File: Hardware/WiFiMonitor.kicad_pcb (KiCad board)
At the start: 2 copper layers, 47.2 x 47.1 mm, 41 parts, among them J1 ADAP_ESP, J2 FTDI, J3 BATT, U1 4N25, U2 4N25, U3 4N25, U4 4N25, U5 U5, U6 AP1117-33, U7 DS3231MZ+

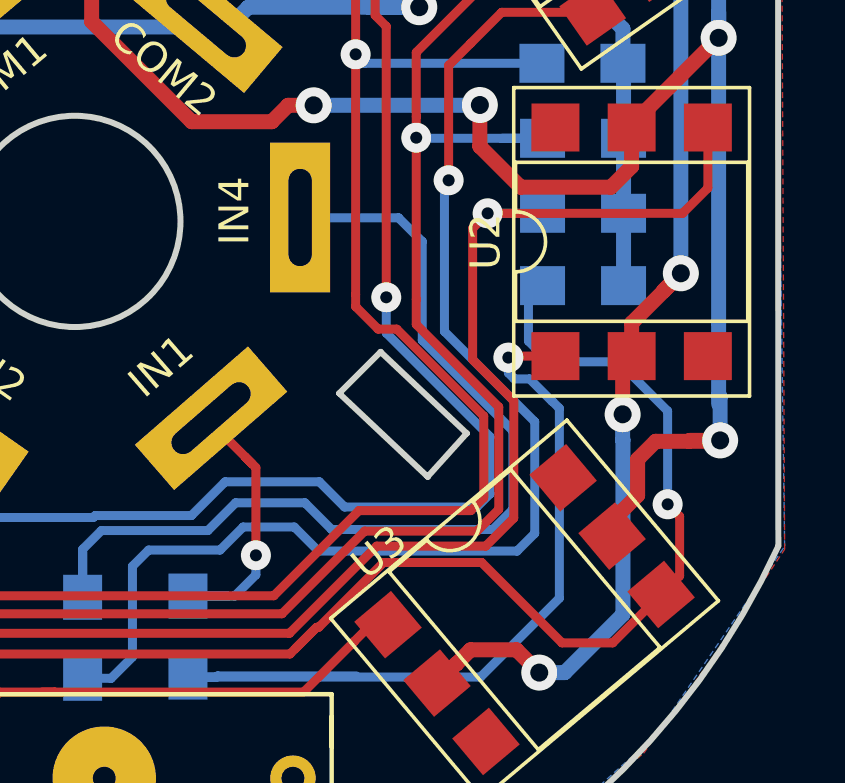
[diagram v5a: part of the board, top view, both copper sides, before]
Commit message: pads4_22
move
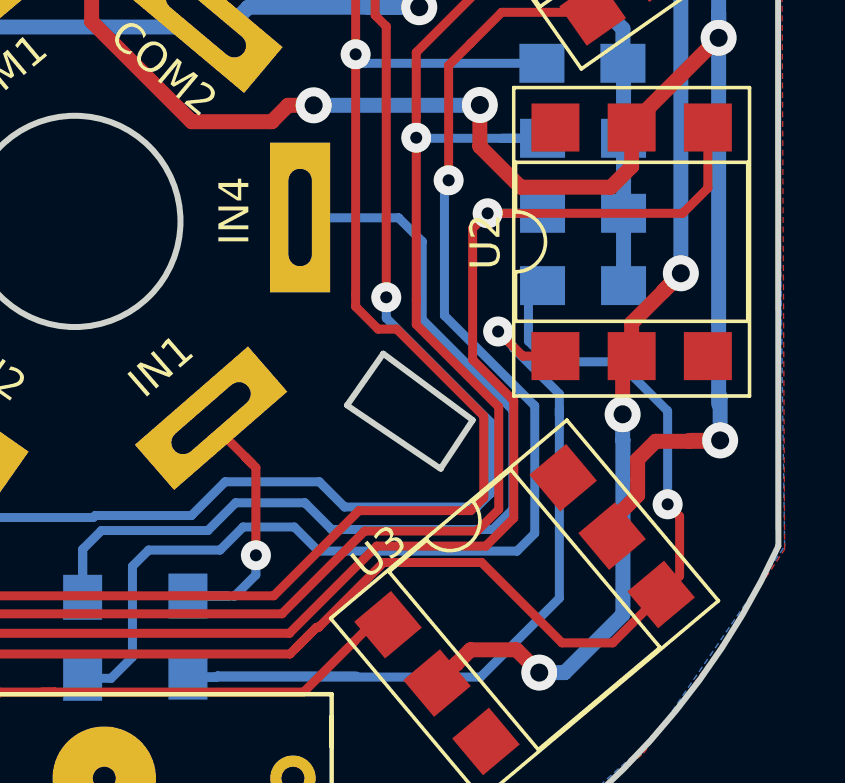
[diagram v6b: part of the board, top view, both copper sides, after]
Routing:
- net Net-(R4-Pad1): track 29.7 -> 31.3 mm
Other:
- outline, holes or cut-outs redrawn
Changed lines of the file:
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@@
     (links 70)
     (no_connects 2)
-    (area 125.549999 67.068854 174.355 116.145)
+    (area 126.056132 67.439999 173.398541 114.790001)
     (thickness 1.6)
     (drawings 29)
-    (tracks 647)
+    (tracks 646)
     (zones 0)
     (modules 41)
@@
   (gr_line (start 136.86 85.59) (end 139.46 87.58) (layer Edge.Cuts) (width 0.2))
   (gr_line (start 136.85 85.59) (end 139.16 82.2) (layer Edge.Cuts) (width 0.2))
-  (gr_line (start 160.0443 95.4057) (end 158.66 96.79) (layer Edge.Cuts) (width 0.2))
-  (gr_line (start 162.92 98.13) (end 160.04 95.41) (layer Edge.Cuts) (width 0.2))
-  (gr_line (start 161.61 99.57) (end 162.91684 98.12062) (layer Edge.Cuts) (width 0.2))
-  (gr_line (start 158.66 96.79) (end 161.62 99.58) (layer Edge.Cuts) (width 0.2))
+  (gr_line (start 160.13 95.47) (end 158.93 97.18) (layer Edge.Cuts) (width 0.2))
+  (gr_line (start 163.11 97.68) (end 160.13 95.47) (layer Edge.Cuts) (width 0.2))
+  (gr_line (start 162.05 99.29) (end 163.11 97.69) (layer Edge.Cuts) (width 0.2))
+  (gr_line (start 158.92 97.19) (end 162.05 99.31) (layer Edge.Cuts) (width 0.2))
   (gr_arc (start 149.72226 91.05258) (end 162.56 113.69) (angle 4.704154906) (layer Edge.Cuts) (width 0.2))
   (gr_arc (start 149.77814 91.05258) (end 173.29854 101.88568) (angle 28.7) (layer Edge.Cuts) (width 0.2))
@@
   (segment (start 140.22 91.07) (end 141.74 91.07) (width 0.3) (layer B.Cu) (net 12))
   (segment (start 150.11 103.59) (end 150.11 101.99) (width 0.3) (layer B.Cu) (net 13))
-  (segment (start 161.43 91.73) (end 160.64 90.94) (width 0.3) (layer B.Cu) (net 13))
+  (segment (start 163.78 101.33) (end 164.45 100.66) (width 0.3) (layer B.Cu) (net 13))
+  (segment (start 164.45 97.35) (end 161.43 94.33) (width 0.3) (layer B.Cu) (net 13))
   (segment (start 150.11 101.99) (end 150.735 101.365) (width 0.3) (layer B.Cu) (net 13))
-  (segment (start 160.64 90.94) (end 157.49 90.94) (width 0.3) (layer B.Cu) (net 13))
   (segment (start 150.735 101.365) (end 154.285 101.365) (width 0.3) (layer B.Cu) (net 13))
   (segment (start 154.285 101.365) (end 155.21 100.44) (width 0.3) (layer B.Cu) (net 13))
-  (segment (start 163.78 101.33) (end 164.45 100.66) (width 0.3) (layer B.Cu) (net 13))
   (segment (start 155.21 100.44) (end 157.52 100.44) (width 0.3) (layer B.Cu) (net 13))
   (segment (start 157.52 100.44) (end 158.41 101.33) (width 0.3) (layer B.Cu) (net 13))
   (segment (start 158.41 101.33) (end 163.78 101.33) (width 0.3) (layer B.Cu) (net 13))
-  (segment (start 164.45 100.66) (end 164.45 98.04) (width 0.3) (layer B.Cu) (net 13))
-  (segment (start 164.45 98.04) (end 161.43 95.02) (width 0.3) (layer B.Cu) (net 13))
-  (segment (start 161.43 95.02) (end 161.43 91.73) (width 0.3) (layer B.Cu) (net 13))
+  (segment (start 164.45 100.66) (end 164.45 97.35) (width 0.3) (layer B.Cu) (net 13))
+  (segment (start 161.43 94.33) (end 161.43 91.73) (width 0.3) (layer B.Cu) (net 13))
+  (segment (start 161.43 91.73) (end 160.64 90.94) (width 0.3) (layer B.Cu) (net 13))
+  (segment (start 160.64 90.94) (end 157.49 90.94) (width 0.3) (layer B.Cu) (net 13))
   (segment (start 150.11 103.59) (end 150.11 102.09) (width 0.3) (layer B.Cu) (net 13))
   (segment (start 141.57 103.24) (end 141.57 104.25) (width 0.3) (layer F.Cu) (net 14))
@@
   (segment (start 137.52 102.76) (end 137.52 103.07) (width 0.3) (layer F.Cu) (net 22))
   (segment (start 143.51 106.21) (end 144.61 106.21) (width 0.3) (layer B.Cu) (net 23))
-  (segment (start 145.945 100.93) (end 150.46288 100.93) (width 0.3) (layer B.Cu) (net 23))
   (segment (start 144.61 106.21) (end 145.11 105.71) (width 0.3) (layer B.Cu) (net 23))
+  (segment (start 160.23 94.28) (end 160.23 93.59) (width 0.3) (layer B.Cu) (net 23))
   (segment (start 145.11 105.71) (end 145.11 101.765) (width 0.3) (layer B.Cu) (net 23))
-  (segment (start 158.84 100.58) (end 163.25 100.58) (width 0.3) (layer B.Cu) (net 23))
-  (segment (start 163.69 100.14) (end 163.69 98.24) (width 0.3) (layer B.Cu) (net 23))
   (segment (start 145.11 101.765) (end 145.945 100.93) (width 0.3) (layer B.Cu) (net 23))
-  (segment (start 150.46288 100.93) (end 150.52789 100.86499) (width 0.3) (layer B.Cu) (net 23))
-  (segment (start 154.86 99.74) (end 158 99.74) (width 0.3) (layer B.Cu) (net 23))
-  (segment (start 163.69 98.24) (end 160.23 94.78) (width 0.3) (layer B.Cu) (net 23))
   (segment (start 150.52789 100.86499) (end 153.73501 100.86499) (width 0.3) (layer B.Cu) (net 23))
+  (segment (start 145.945 100.93) (end 150.46288 100.93) (width 0.3) (layer B.Cu) (net 23))
   (segment (start 153.73501 100.86499) (end 154.86 99.74) (width 0.3) (layer B.Cu) (net 23))
+  (segment (start 150.46288 100.93) (end 150.52789 100.86499) (width 0.3) (layer B.Cu) (net 23))
+  (segment (start 154.86 99.74) (end 158 99.74) (width 0.3) (layer B.Cu) (net 23))
   (segment (start 158 99.74) (end 158.84 100.58) (width 0.3) (layer B.Cu) (net 23))
+  (segment (start 158.84 100.58) (end 163.25 100.58) (width 0.3) (layer B.Cu) (net 23))
   (segment (start 163.25 100.58) (end 163.69 100.14) (width 0.3) (layer B.Cu) (net 23))
-  (segment (start 160.23 94.78) (end 160.23 93.59) (width 0.3) (layer B.Cu) (net 23))
+  (segment (start 163.69 100.14) (end 163.69 97.74) (width 0.3) (layer B.Cu) (net 23))
+  (segment (start 163.69 97.74) (end 160.23 94.28) (width 0.3) (layer B.Cu) (net 23))
   (segment (start 160.23 93.59) (end 160.23 84.56) (width 0.3) (layer F.Cu) (net 23))
   (segment (start 160.23 84.56) (end 159.86 84.19) (width 0.3) (layer F.Cu) (net 23))
@@
   (segment (start 159.160134 105.061824) (end 159.79869 104.423268) (width 0.3) (layer F.Cu) (net 24))
   (segment (start 150.11 106.29) (end 151.06 106.29) (width 0.3) (layer B.Cu) (net 25))
-  (segment (start 165.18 101.46) (end 165.18 97.738002) (width 0.3) (layer B.Cu) (net 25))
+  (segment (start 157.97 102.05) (end 164.59 102.05) (width 0.3) (layer B.Cu) (net 25))
   (segment (start 151.06 106.29) (end 151.77 105.58) (width 0.3) (layer B.Cu) (net 25))
-  (segment (start 164.59 102.05) (end 165.18 101.46) (width 0.3) (layer B.Cu) (net 25))
-  (segment (start 151.77 105.58) (end 151.77 102.555) (width 0.3) (layer B.Cu) (net 25))
   (segment (start 151.77 102.555) (end 152.31 102.015) (width 0.3) (layer B.Cu) (net 25))
+  (segment (start 151.77 105.58) (end 151.77 102.555) (width 0.3) (layer B.Cu) (net 25))
   (segment (start 152.31 102.015) (end 154.69212 102.015) (width 0.3) (layer B.Cu) (net 25))
   (segment (start 154.69212 102.015) (end 155.46 101.24712) (width 0.3) (layer B.Cu) (net 25))
   (segment (start 155.46 101.24712) (end 157.16712 101.24712) (width 0.3) (layer B.Cu) (net 25))
   (segment (start 157.16712 101.24712) (end 157.97 102.05) (width 0.3) (layer B.Cu) (net 25))
-  (segment (start 157.97 102.05) (end 164.59 102.05) (width 0.3) (layer B.Cu) (net 25))
-  (segment (start 165.18 97.738002) (end 162.17 94.728002) (width 0.3) (layer B.Cu) (net 25))
-  (segment (start 162.17 94.728002) (end 162.17 89.83) (width 0.3) (layer B.Cu) (net 25))
+  (segment (start 162.17 94.198001) (end 162.17 89.83) (width 0.3) (layer B.Cu) (net 25))
+  (segment (start 164.59 102.05) (end 165.18 101.46) (width 0.3) (layer B.Cu) (net 25))
+  (segment (start 165.18 101.46) (end 165.18 97.208001) (width 0.3) (layer B.Cu) (net 25))
+  (segment (start 165.18 97.208001) (end 162.17 94.198001) (width 0.3) (layer B.Cu) (net 25))
   (segment (start 162.17 89.83) (end 162.31 89.69) (width 0.3) (layer B.Cu) (net 25))
   (segment (start 163.05 85.12) (end 164.08 84.09) (width 0.3) (layer F.Cu) (net 25))
@@
   (via (at 162.31 89.69) (size 1) (drill 0.4) (layers F.Cu B.Cu) (net 25))
   (segment (start 164.08 84.09) (end 167.11 84.09) (width 0.3) (layer F.Cu) (net 25))
-  (segment (start 166 103.62) (end 166 97.29) (width 0.3) (layer B.Cu) (net 26))
-  (segment (start 165.75 97.05) (end 165.76 97.05) (width 0.3) (layer B.Cu) (net 26))
-  (segment (start 165.76 97.05) (end 166 97.29) (width 0.3) (layer B.Cu) (net 26))
+  (segment (start 166 103.62) (end 166 97.52) (width 0.3) (layer B.Cu) (net 26))
+  (segment (start 164.46 95.27) (end 166 96.81) (width 0.3) (layer B.Cu) (net 26))
+  (segment (start 166 97.52) (end 166 97.29) (width 0.3) (layer B.Cu) (net 26))
+  (segment (start 166 96.81) (end 166 97.52) (width 0.3) (layer B.Cu) (net 26))
+  (segment (start 163.960001 94.73) (end 164.46 95.229999) (width 0.3) (layer B.Cu) (net 26))
+  (segment (start 164.46 95.229999) (end 164.46 95.27) (width 0.3) (layer B.Cu) (net 26))
+  (segment (start 165.87 95.55) (end 164.780001 95.55) (width 0.3) (layer F.Cu) (net 26))
+  (segment (start 164.780001 95.55) (end 163.960001 94.73) (width 0.3) (layer F.Cu) (net 26))
+  (via (at 163.960001 94.73) (size 1) (drill 0.4) (layers F.Cu B.Cu) (net 26))
   (segment (start 153.62 106.25) (end 163.37 106.25) (width 0.3) (layer B.Cu) (net 26))
   (segment (start 163.37 106.25) (end 166 103.62) (width 0.3) (layer B.Cu) (net 26))
-  (segment (start 164.5 96.31) (end 164.3 96.11) (width 0.3) (layer B.Cu) (net 26))
-  (segment (start 165.75 97.05) (end 165.01 96.31) (width 0.3) (layer B.Cu) (net 26))
-  (segment (start 165.01 96.31) (end 164.5 96.31) (width 0.3) (layer B.Cu) (net 26))
-  (segment (start 164.3 96.11) (end 164.3 95.6) (width 0.3) (layer B.Cu) (net 26))
-  (segment (start 165.87 95.55) (end 164.35 95.55) (width 0.3) (layer F.Cu) (net 26))
-  (segment (start 164.35 95.55) (end 164.3 95.6) (width 0.3) (layer F.Cu) (net 26))
-  (via (at 164.3 95.6) (size 1) (drill 0.4) (layers F.Cu B.Cu) (net 26))
   (segment (start 159.23 106.21) (end 154.61 106.21) (width 0.3) (layer B.Cu) (net 26))
   (segment (start 154.61 106.21) (end 154.57 106.25) (width 0.3) (layer B.Cu) (net 26))
